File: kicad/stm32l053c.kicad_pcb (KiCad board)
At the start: 2 copper layers, 90 x 70 mm, 58 parts, among them J1 Water_Level, J2 Motion, J3 Door, J4 Door_Led, J5 AIN3, J6 Pump, J7 BATTERY, P1 SWD, Q1 Q_NMOS_GSD, Q2 Q_PMOS_GSD, U1 MCP1703A-5002_SOT223, U2 STM32L053C8_LQFP48, U3 ADS1015, U4 UFL_SMA, U5 RFM92/95, U6 MCP1703A-3302_SOT223

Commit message: Power layout
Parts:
- removed J5: AIN3, Connector_PinHeader_2.54mm:PinHeader_1x02_P2.54mm_Vertical
- removed R14: 620K, Resistor_SMD:R_0805_2012Metric_Pad1.15x1.40mm_HandSolder
- removed R15: 100K, Resistor_SMD:R_0805_2012Metric_Pad1.15x1.40mm_HandSolder
- F1, Q2: moved to B.Cu
- R10, R4: moved to F.Cu
- moved R11 66.4 mm to (94.7, 105.4)
- moved R6 55.0 mm to (93.8, 77.8), turned to 270 degrees
- moved R7 53.1 mm to (94.6, 69.8), turned to 0 degrees
- moved R8 48.6 mm to (137.9, 109.4), turned to 0 degrees
- moved R9 42.5 mm to (137.9, 105.0), turned to 180 degrees
- moved D1 29.4 mm to (161.7, 117.7)
- moved R1 29.0 mm to (161.7, 114.4), turned to 0 degrees
- moved R21 13.1 mm to (127.1, 86.6), turned to 0 degrees
- moved C9 11.0 mm to (123.0, 85.0), turned to 0 degrees
- moved C7 7.50 mm to (152.8, 66.0), turned to 0 degrees
- moved C6 6.42 mm to (123.0, 88.5), turned to 0 degrees
- moved R4 6.09 mm to (140.9, 79.5), turned to 180 degrees
- moved C4 6.02 mm to (123.0, 81.5), turned to 0 degrees
- moved R10 5.45 mm to (140.9, 77.4), turned to 0 degrees
- moved F1 3.83 mm to (132.9, 107.2), turned to 270 degrees
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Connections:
- C12 pad 2: Net-(C12-Pad2) -> Earth
- C5 pad 2: Net-(C12-Pad2) -> Earth
- R8 pad 2: /AIN2 -> /AIN3
- R9 pad 1: /AIN2 -> /AIN3
- U2 pad 10: WATER_TEMP -> Net-(U2-Pad10)
- U2 pad 11: WATER_LEVEL -> Net-(U2-Pad11)
- U2 pad 14: SENSOR_PWR -> Net-(U2-Pad14)
- U2 pad 38: Net-(U2-Pad38) -> WATER_LEVEL
- U2 pad 39: Net-(U2-Pad39) -> SENSOR_PWR
- U3 pad 6: /AIN2 -> WATER_TEMP
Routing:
- net Earth: track 90.0 -> 257.0 mm, vias 5 -> 6
- net +5V: track 0.00 -> 85.6 mm
- net +3V3: track 77.5 -> 162.4 mm, vias 4 -> 3
- net WATER_TEMP: track 0.00 -> 73.9 mm, vias 0 -> 2
- net SENSOR_PWR: track 0.00 -> 66.5 mm, vias 0 -> 1
- net WATER_LEVEL: track 0.00 -> 58.1 mm, vias 0 -> 1
- net /AIN3: track 0.00 -> 52.0 mm, vias 0 -> 2
- net Net-(C12-Pad1): track 0.00 -> 50.6 mm
- net LED: track 5.93 -> 38.4 mm
- net /AIN0: track 0.00 -> 31.2 mm
- net /AIN1: track 0.00 -> 28.5 mm
- net /BATT: track 20.9 -> 8.01 mm, vias 1 -> 0
- net Net-(D3-Pad2): track 0.00 -> 5.39 mm
- net +BATT: track 0.00 -> 4.23 mm
- net Net-(J4-Pad2): track 0.00 -> 3.62 mm
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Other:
- board text added: "-"
- board text added: "5V+"
- board text removed: "RX"
- board text removed: "TX"

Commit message: Changed the overvoltage protection
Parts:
- removed C9: 10uF, Capacitor_SMD:C_0805_2012Metric_Pad1.15x1.40mm_HandSolder
- removed R21: 1K, Resistor_SMD:R_0603_1608Metric_Pad1.05x0.95mm_HandSolder
- added RV1: 18V, Varistor:RV_Disc_D7mm_W5.4mm_P5mm, F.Cu at (132.5, 115.0)
- D3: value 3V6 -> 16V
- moved D3 39.3 mm to (112.5, 120.0)
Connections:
- C12 pad 1: Net-(C12-Pad1) -> /BATT
- C5 pad 1: Net-(C12-Pad1) -> /BATT
- D3 pad 1: +3V3 -> /BATT
- D3 pad 2: Net-(D3-Pad2) -> Earth
- F1 pad 1: Net-(C12-Pad1) -> Net-(F1-Pad1)
- F1 pad 2: /BATT -> +BATT
- Q2 pad 3: +BATT -> Net-(F1-Pad1)
- R8 pad 1: /BATT -> /AIN3
- R8 pad 2: /AIN3 -> /BATT
- U1 pad 1: Net-(C12-Pad1) -> /BATT
- U2 pad 10: Net-(U2-Pad10) -> (no net)
- U2 pad 11: Net-(U2-Pad11) -> (no net)
- U2 pad 13: USART2_RX -> (no net)
- U2 pad 14: Net-(U2-Pad14) -> (no net)
- U2 pad 17: Net-(U2-Pad17) -> (no net)
- U2 pad 29: Net-(U2-Pad29) -> (no net)
- U2 pad 3: Net-(U2-Pad3) -> (no net)
- U2 pad 30: Net-(U2-Pad30) -> (no net)
- U2 pad 31: Net-(U2-Pad31) -> (no net)
- U2 pad 4: Net-(U2-Pad4) -> (no net)
- U2 pad 40: Net-(U2-Pad40) -> (no net)
- U2 pad 45: Net-(U2-Pad45) -> (no net)
- U2 pad 46: Net-(U2-Pad46) -> (no net)
- U2 pad 5: Net-(U2-Pad5) -> (no net)
- U2 pad 6: Net-(U2-Pad6) -> (no net)
- U5 pad 11: Net-(U5-Pad11) -> (no net)
- U5 pad 12: Net-(U5-Pad12) -> (no net)
- U5 pad 15: Net-(U5-Pad15) -> (no net)
- U5 pad 16: Net-(U5-Pad16) -> (no net)
- U5 pad 7: Net-(U5-Pad7) -> (no net)
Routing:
- net +3V3: track 162.4 -> 156.9 mm
- net Net-(D3-Pad2): track 5.39 -> 0.00 mm
- net Earth: track 257.0 -> 254.2 mm

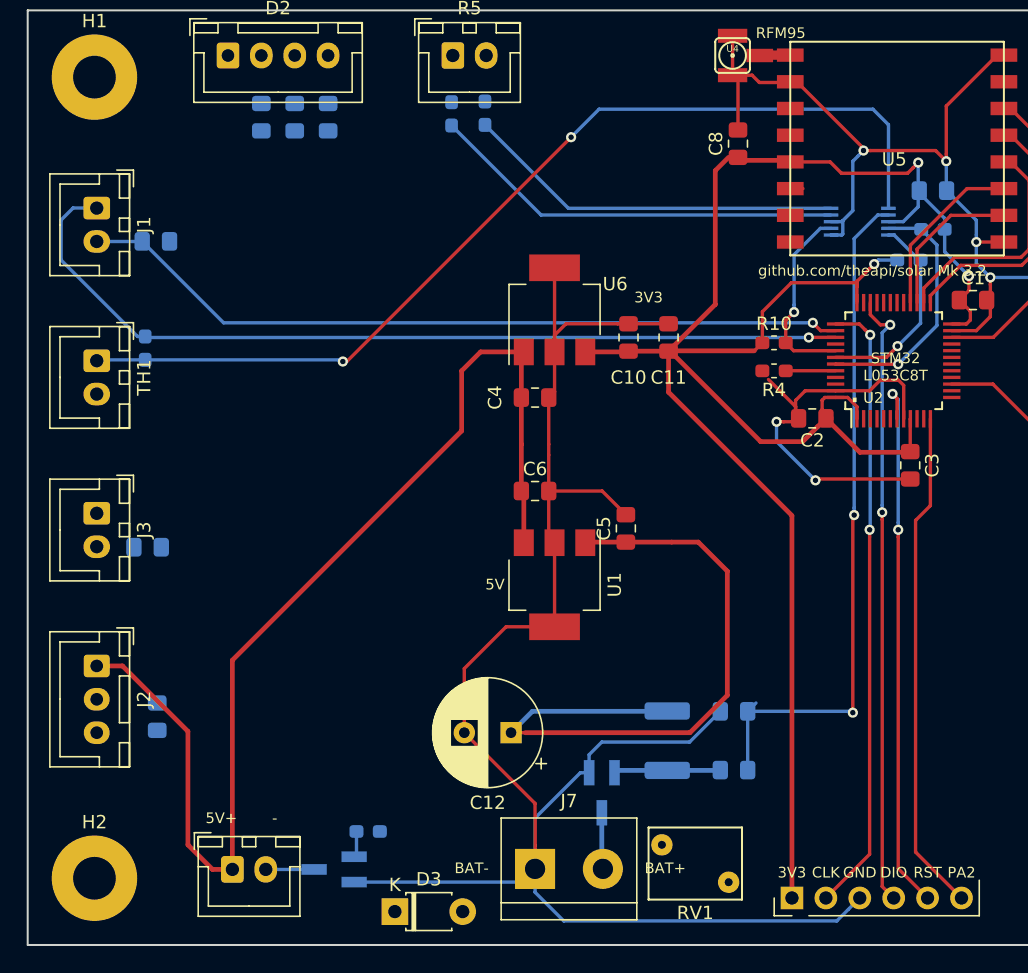
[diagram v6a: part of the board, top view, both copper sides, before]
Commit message: Reassign ADC pins
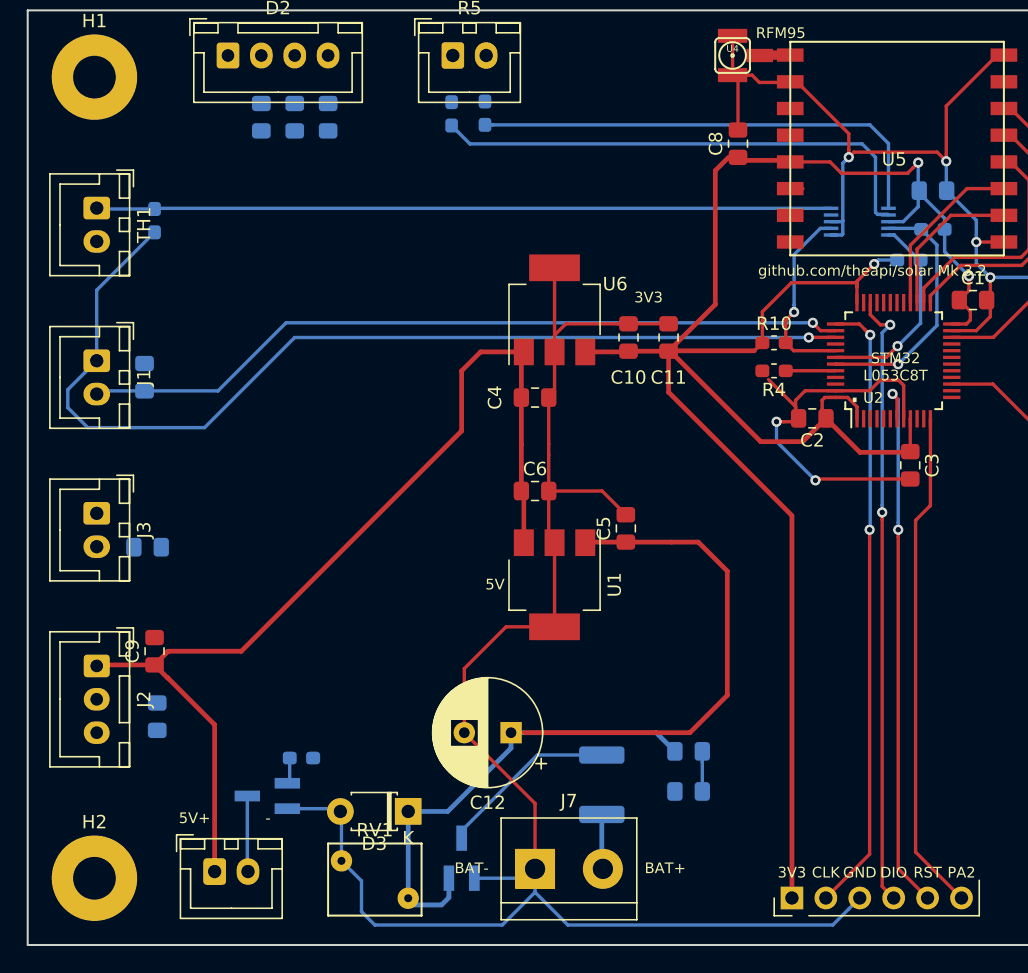
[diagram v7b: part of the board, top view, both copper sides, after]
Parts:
- added C9: 10uF, Capacitor_SMD:C_0805_2012Metric_Pad1.15x1.40mm_HandSolder, F.Cu at (94.5, 100.5)
- moved RV1 19.4 mm to (113.5, 119.0), turned to 180 degrees
- moved Q2 11.6 mm to (117.5, 116.0), turned to 90 degrees
- moved J1 11.4 mm to (90.2, 78.7)
- moved TH1 11.4 mm to (90.2, 67.3)
- moved R7 10.2 mm to (93.8, 80.0), turned to 90 degrees
- moved R6 9.58 mm to (94.5, 68.2), turned to 90 degrees
- moved D3 7.57 mm to (113.5, 112.5), turned to 180 degrees
- moved Q1 7.43 mm to (103.0, 111.3)
- moved R13 7.43 mm to (105.5, 108.5)
- moved R9 6.90 mm to (134.5, 111.0)
- moved F1 5.91 mm to (128.0, 110.5)
- moved R8 3.68 mm to (134.5, 108.0), turned to 180 degrees
- moved J4 1.34 mm to (99.0, 117.0)
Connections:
- R19 pad 1: /AIN1 -> /AIN2
- R20 pad 1: /AIN0 -> /AIN3
- R8 pad 1: /AIN3 -> /BATT_V
- R9 pad 1: /AIN3 -> /BATT_V
- U2 pad 10: (no net) -> Net-(U2-Pad10)
- U2 pad 11: (no net) -> Net-(U2-Pad11)
- U2 pad 13: (no net) -> USART2_RX
- U2 pad 14: (no net) -> Net-(U2-Pad14)
- U2 pad 17: (no net) -> Net-(U2-Pad17)
- U2 pad 29: (no net) -> Net-(U2-Pad29)
- U2 pad 3: (no net) -> Net-(U2-Pad3)
- U2 pad 30: (no net) -> Net-(U2-Pad30)
- U2 pad 31: (no net) -> Net-(U2-Pad31)
- U2 pad 4: (no net) -> Net-(U2-Pad4)
- U2 pad 40: (no net) -> Net-(U2-Pad40)
- U2 pad 45: (no net) -> Net-(U2-Pad45)
- U2 pad 46: (no net) -> Net-(U2-Pad46)
- U2 pad 5: (no net) -> Net-(U2-Pad5)
- U2 pad 6: (no net) -> Net-(U2-Pad6)
- U3 pad 4: /AIN0 -> /BATT_V
- U3 pad 5: /AIN1 -> WATER_TEMP
- U3 pad 6: WATER_TEMP -> /AIN2
- U5 pad 11: (no net) -> Net-(U5-Pad11)
- U5 pad 12: (no net) -> Net-(U5-Pad12)
- U5 pad 15: (no net) -> Net-(U5-Pad15)
- U5 pad 16: (no net) -> Net-(U5-Pad16)
- U5 pad 7: (no net) -> Net-(U5-Pad7)
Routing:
- net /BATT: track 8.01 -> 73.3 mm
- net Net-(C12-Pad1): track 50.6 -> 0.00 mm
- net /AIN2: track 0.00 -> 35.7 mm
- net /AIN0: track 31.2 -> 0.00 mm
- net /AIN1: track 28.5 -> 0.00 mm
- net WATER_TEMP: track 73.9 -> 55.2 mm, vias 2 -> 0
- net /AIN3: track 52.0 -> 37.9 mm, vias 2 -> 0
- net Net-(F1-Pad1): track 0.00 -> 13.4 mm
- net SENSOR_PWR: track 66.5 -> 76.7 mm
- net +5V: track 85.6 -> 76.2 mm
- net /BATT_V: track 0.00 -> 3.00 mm
- net Earth: track 254.2 -> 251.9 mm
- net Net-(J4-Pad2): track 3.62 -> 5.68 mm

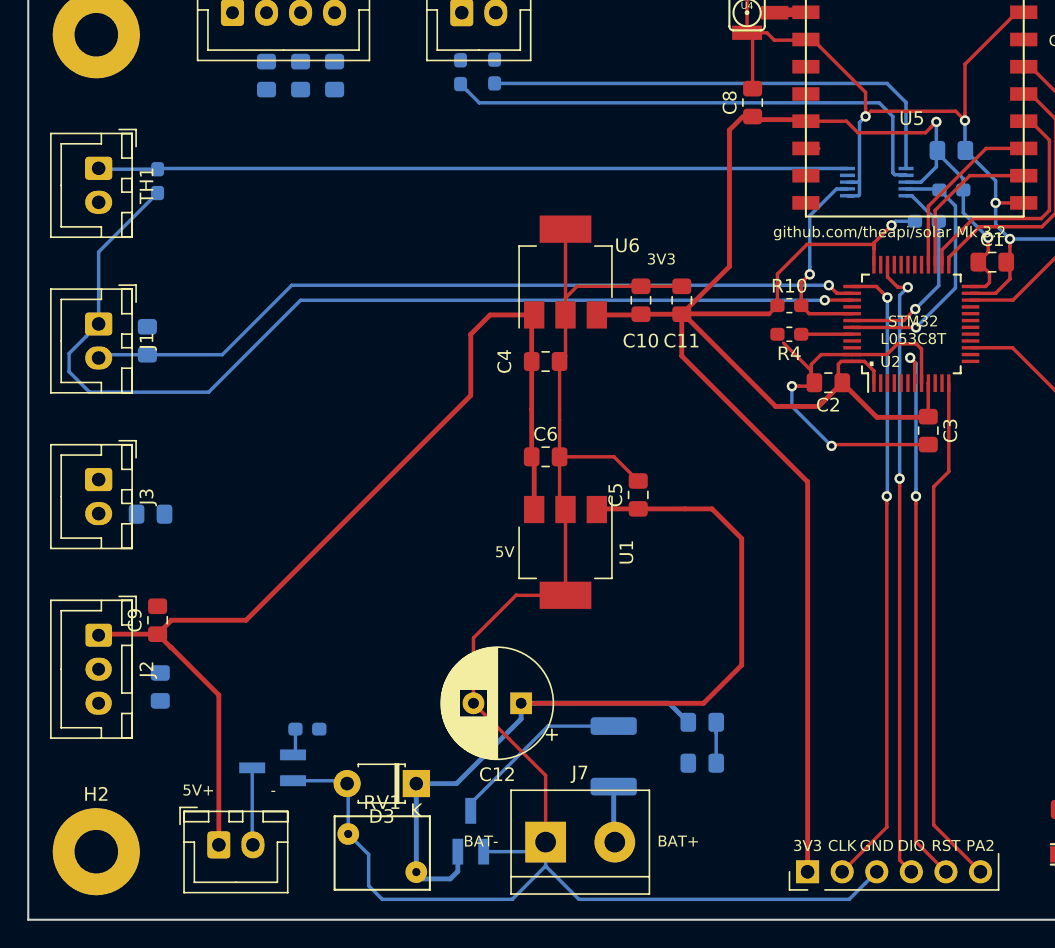
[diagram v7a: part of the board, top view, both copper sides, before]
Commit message: Moved the ADC
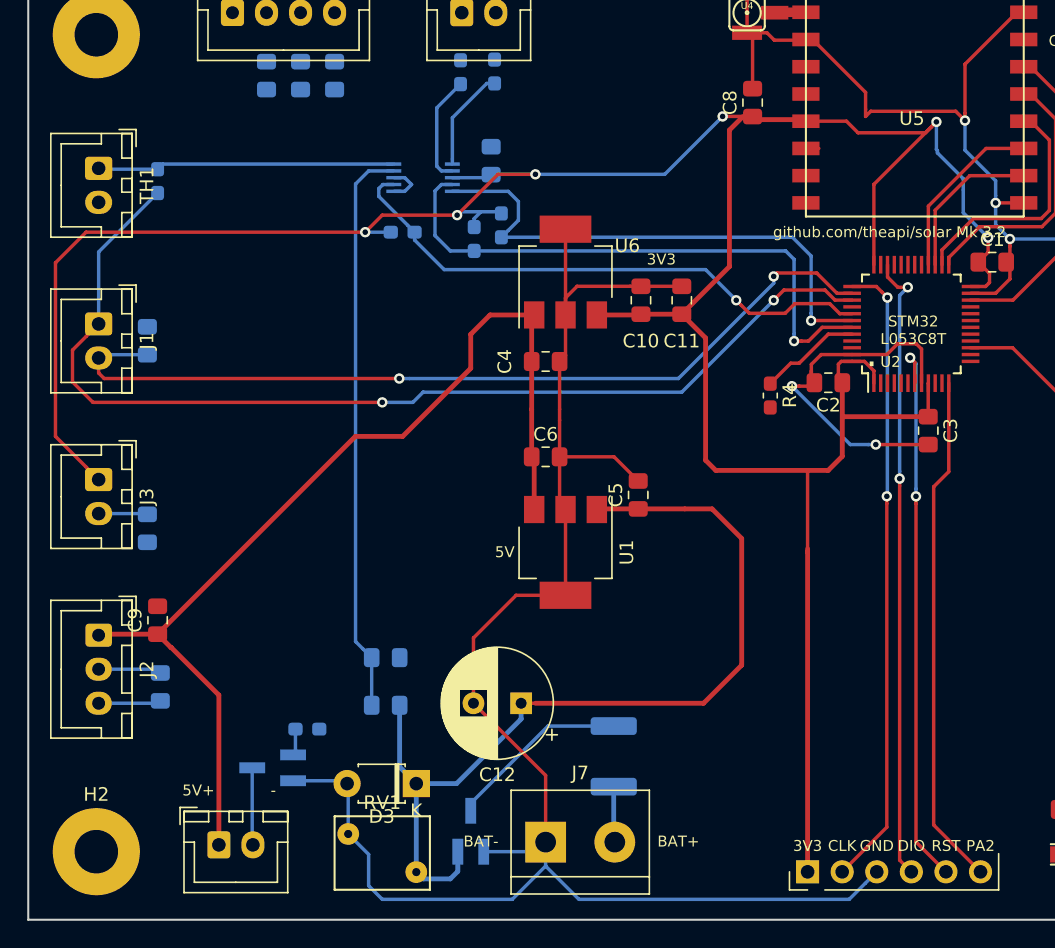
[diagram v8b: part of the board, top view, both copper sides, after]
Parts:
- R10: moved to B.Cu
- moved R2 35.2 mm to (117.8, 72.5), turned to 270 degrees
- moved C7 33.8 mm to (119.0, 66.8), turned to 90 degrees
- moved U3 33.3 mm to (114.0, 68.0)
- moved R3 31.3 mm to (119.8, 71.5), turned to 270 degrees
- moved R10 28.9 mm to (112.5, 72.0)
- moved R9 24.5 mm to (111.2, 103.2), turned to 0 degrees
- moved R8 23.3 mm to (111.2, 106.8), turned to 0 degrees
- moved R4 4.71 mm to (139.5, 84.0), turned to 270 degrees
- moved R12 1.07 mm to (93.8, 93.8), turned to 270 degrees
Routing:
- net +3V3: track 156.9 -> 224.1 mm, vias 3 -> 6
- net /BATT_V: track 3.00 -> 42.0 mm
- net WATER_TEMP: track 55.2 -> 22.2 mm
- net /AIN3: track 37.9 -> 8.05 mm
- net /AIN2: track 35.7 -> 7.55 mm
- net ADC_RDY: track 14.4 -> 41.1 mm
- net I2C1_SCL: track 15.3 -> 39.4 mm
- net I2C1_SDA: track 19.0 -> 42.5 mm
- net WATER_LEVEL: track 57.8 -> 64.4 mm, vias 1 -> 2
- net /BATT: track 73.3 -> 66.7 mm
- net MOTION: track 0.00 -> 4.64 mm
- net Earth: track 251.9 -> 247.5 mm, vias 6 -> 5
- net /BOOT0: track 3.74 -> 7.52 mm
- net DOOR: track 0.00 -> 3.60 mm
- net SENSOR_PWR: track 76.7 -> 78.1 mm, vias 1 -> 2
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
